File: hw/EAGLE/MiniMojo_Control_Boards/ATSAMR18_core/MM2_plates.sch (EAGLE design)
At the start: 54 parts, among them J1 CORTEX_DEBUGSMD, Q1 MOSFET-NCHANNEL2N7002PW, U1 3.3V, U2 EM406

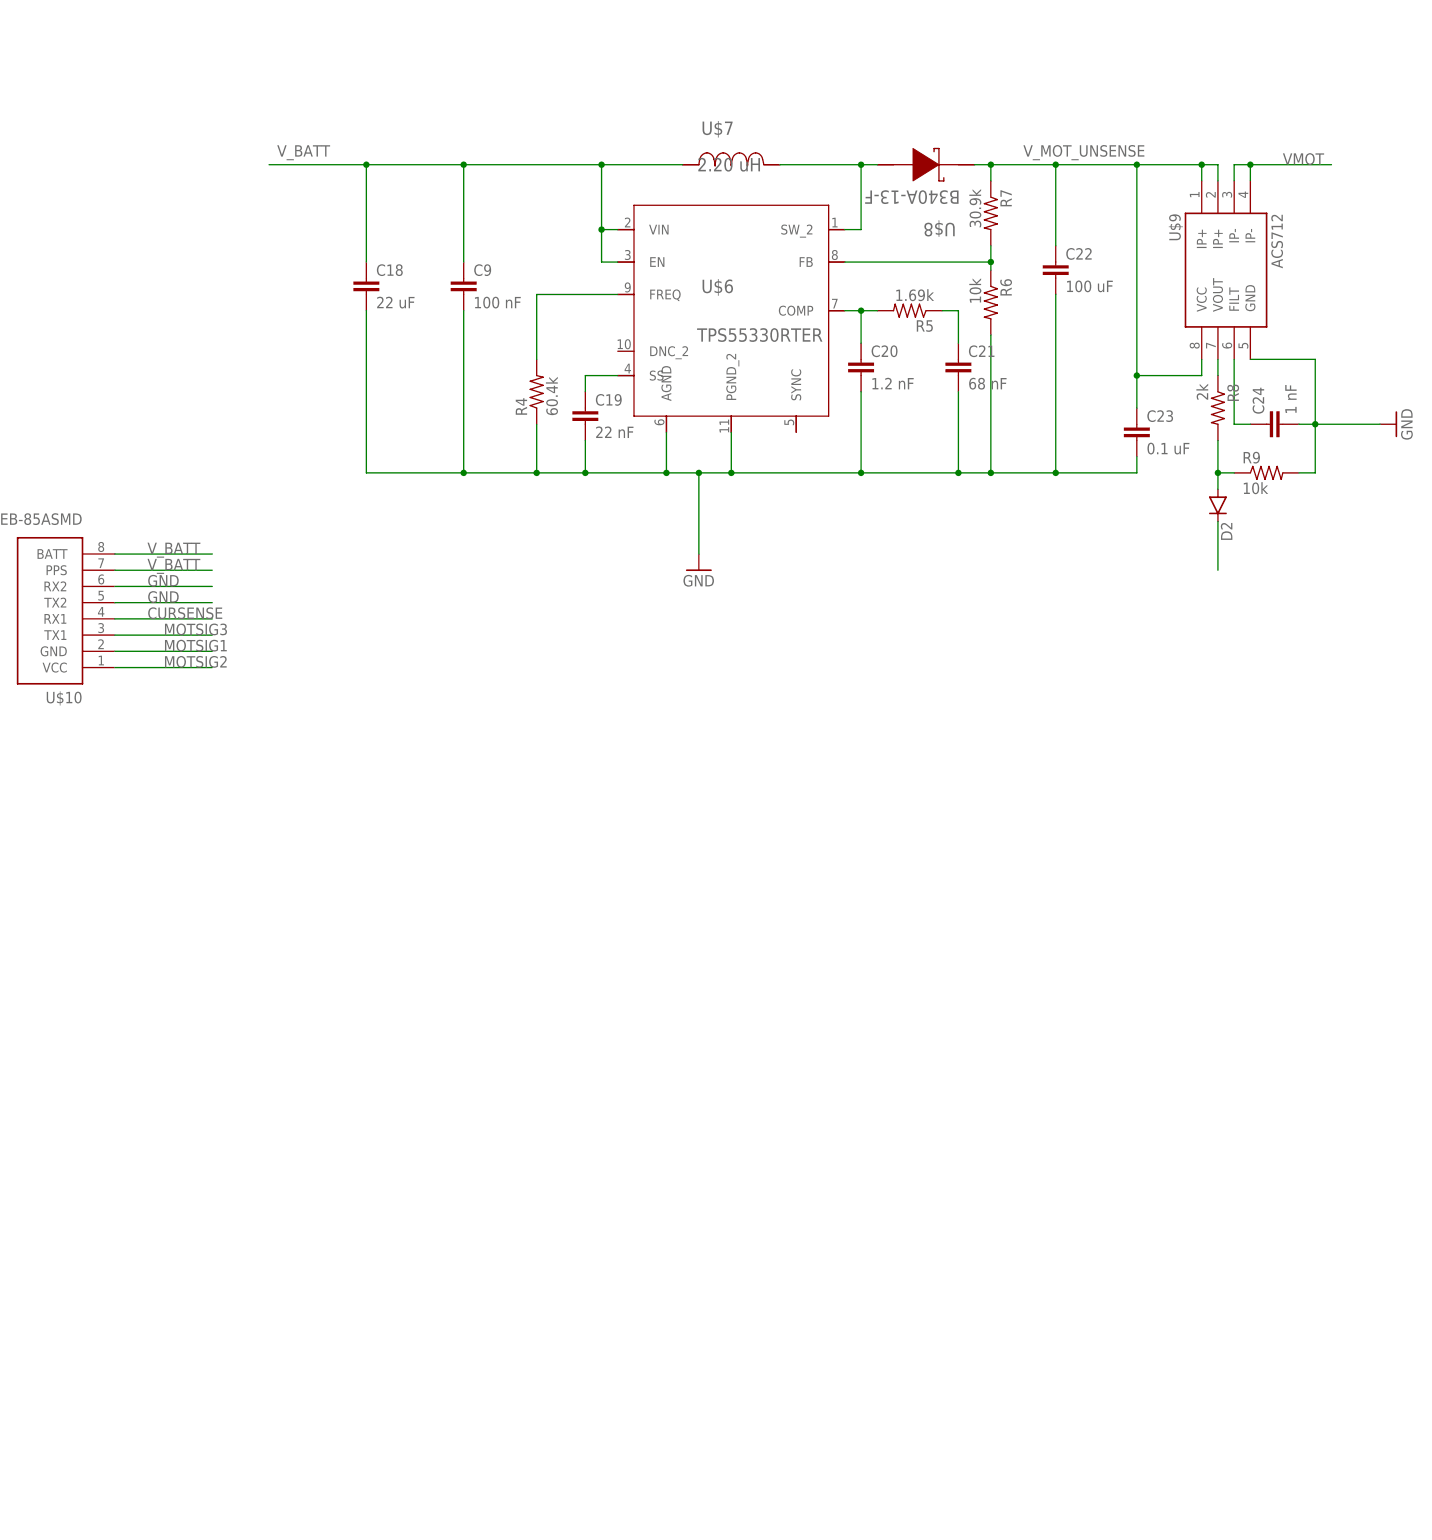
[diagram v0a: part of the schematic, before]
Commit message: Made TPS61089 mods
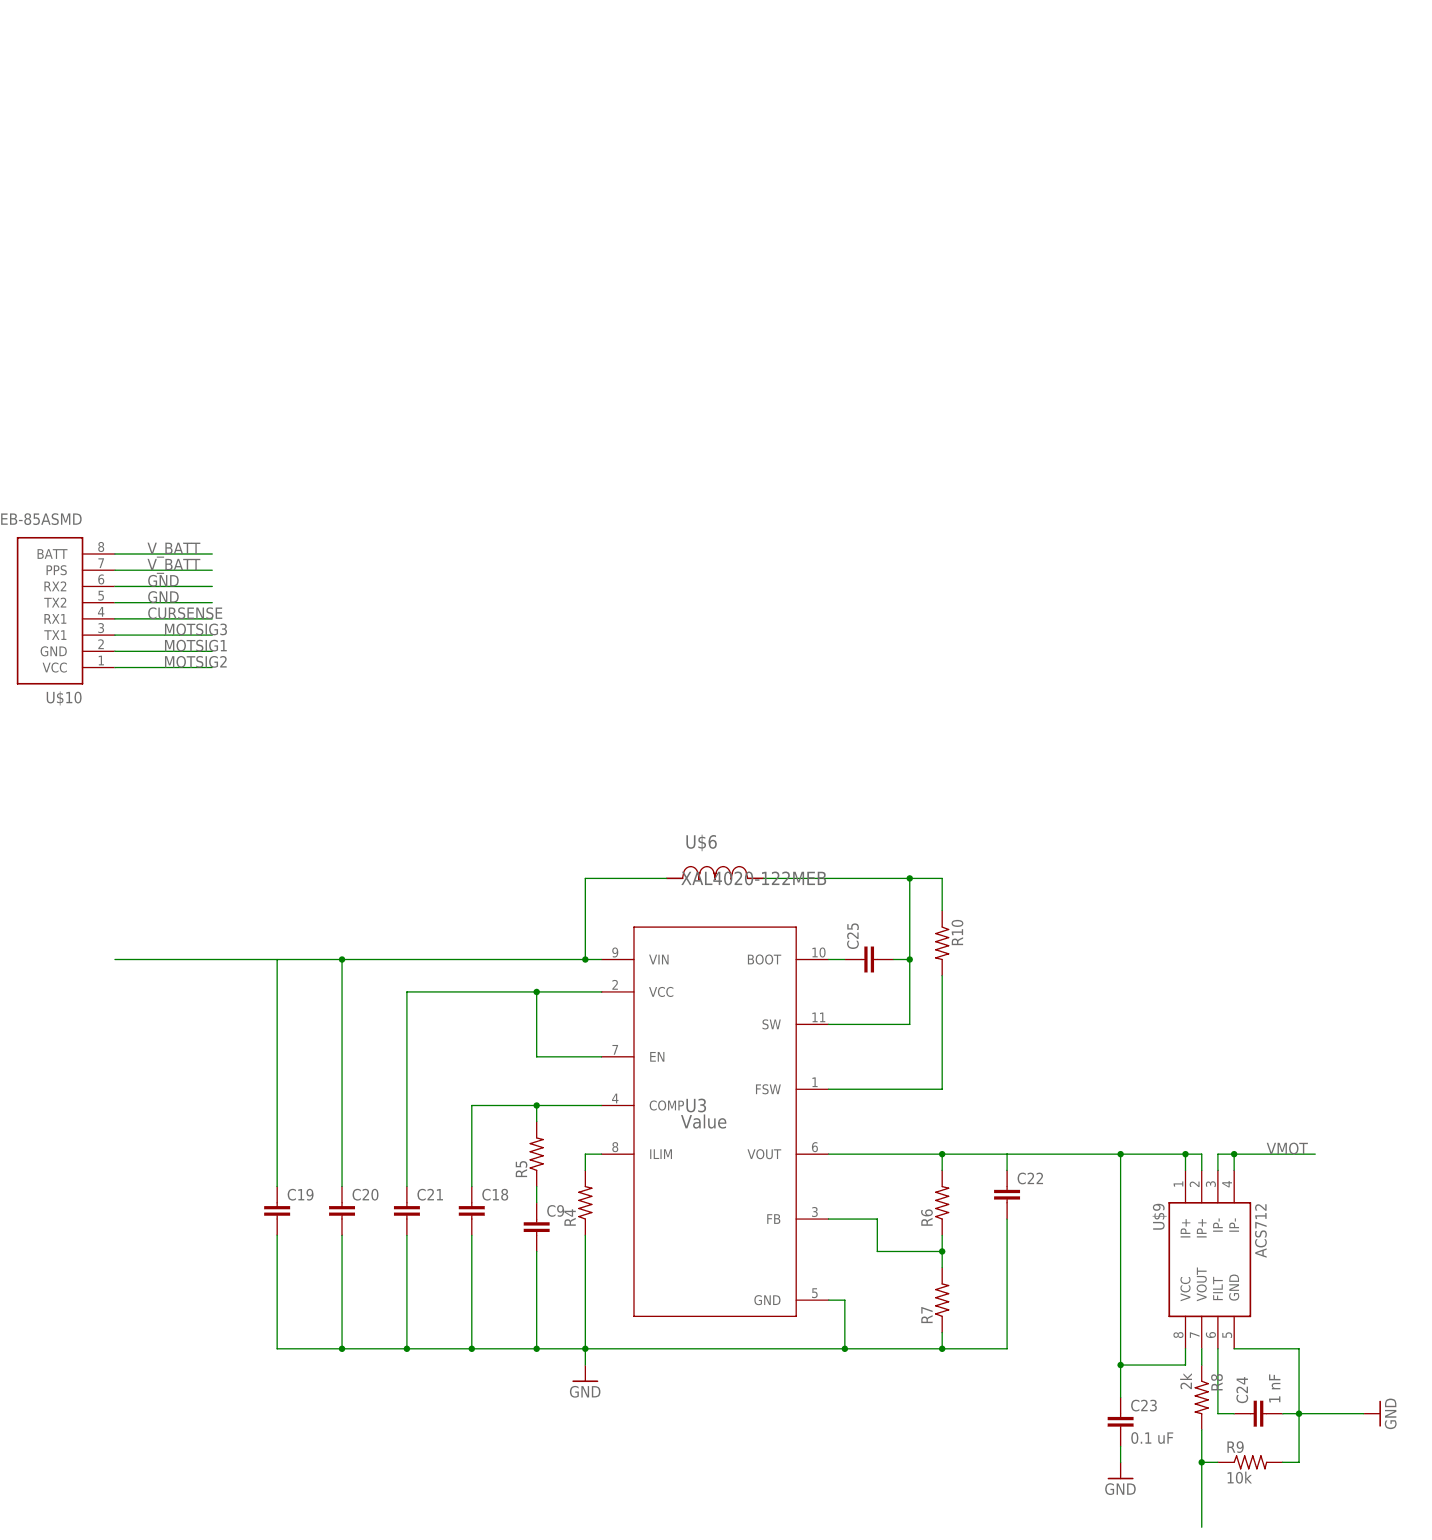
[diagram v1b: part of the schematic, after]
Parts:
- removed D2: (no value), SparkFun-DiscreteSemi:DIODESOD123
- removed U$7: 2.20 uH, TPS55330_libref:SRP4020-2R2M
- removed U$8: B340A-13-F, TPS55330_libref:B340A-13-F
- added C25: (no value), SparkFun-Passives:CAP0402-CAP
- added R10: (no value), SparkFun-Resistors:RESISTOR1206
- added U3: Value, TPS61089RNRR_4.8V:TPS61089RNRR
- C18: value 22 uF -> (none); device SparkFun-Passives:CAP1206 -> SparkFun-Passives:CAP0805
- C19: value 22 nF -> (none); device SparkFun-Passives:CAP0402-CAP -> SparkFun-Passives:CAP1206
- C20: value 1.2 nF -> (none)
- C21: value 68 nF -> (none); device SparkFun-Passives:CAP0402-CAP -> SparkFun-Passives:CAP0603-CAP
- C22: value 100 uF -> (none)
- C9: value 100 nF -> (none); device SparkFun-Passives:CAP0402-CAP -> SparkFun-Passives:CAP0805
- R4: value 60.4k -> (none); device SparkFun-Passives:RESISTOR0402-RES -> SparkFun-Resistors:RESISTOR1206
- R5: value 1.69k -> (none); device SparkFun-Passives:RESISTOR0402-RES -> SparkFun-Resistors:RESISTOR0402
- R6: value 10k -> (none); device SparkFun-Passives:RESISTOR0402-RES -> SparkFun-Resistors:RESISTOR0402
- R7: value 30.9k -> (none); device SparkFun-Passives:RESISTOR0402-RES -> SparkFun-Passives:RESISTOR0603-RES
- U$6: value TPS55330RTER -> XAL4020-122MEB; device TPS55330_libref:TPS55330RTER -> TPS61089RNRR_4.8V:XAL4020-122MEB
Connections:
- removed net N$13: C19.1, U$6.SS
- removed net N$18: R4.2, U$6.FREQ
- removed net N$4: U$6.SW_2, U$7.2, U$8.A
- removed net N$5: D2.A, R8.2, R9.1
- removed net N$9: C20.1, R5.2, U$6.COMP
- new net N$19: C21.1, U3.EN, U3.VCC
- new net N$27: C25.1, U3.BOOT
- new net N$28: C25.2, R10.1, U$6.2, U3.SW
- new net N$29: R10.2, U3.FSW
- new net N$3: R4.2, U3.ILIM
- new net N$31: R6.1, R7.2, U3.FB
- net CURSENSE: now also R8.2, R9.1; no longer D2.C
- net GND: now also R7.1, U3.GND; no longer R6.2, U$6.AGND, U$6.PGND_2
- net N$14: now also C9.1; no longer C21.1
- net N$15: now also C18.1, R5.2, U3.COMP; no longer R6.1, R7.2, U$6.FB
- net V_BATT: now also C19.1, C20.1, U$6.1, U3.VIN; no longer C18.1, C9.1, U$6.EN, U$6.VIN, U$7.1
- net V_MOT_UNSENSE: now also R6.2, U3.VOUT; no longer R7.1, U$8.K
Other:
- moved on the sheet: C18, C19, C20, C21, C22, C23, C24, C9, R4, R5, R6, R7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

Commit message: added TPS61089 w/ Tiny841
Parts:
- removed U$6: XAL4020-122MEB, TPS61089RNRR_4.8V:XAL4020-122MEB
- added J3: (no value), CSL_Components:M06SMD-1MM
- added Q2, Q3: MOSFET-NCHANNELAO3404A, SparkFun-DiscreteSemi:MOSFET-NCHANNELAO3404A
- added R11, R13, R14: 10k, SparkFun-Passives:RESISTOR0402-RES
- added U10: ATTINY84ATTINY84-20MU, SparkFun-DigitalIC:ATTINY84ATTINY84-20MU
- added U4: EM406, SparkFun-Connectors:EM406
- added Y1: 16MHZ, SparkFun-FreqCtrl:RESONATOR16MHZ
- C18: value (none) -> 62 pF
- C19, C22: value (none) -> 47 uF
- C20, C25: value (none) -> 100 nF
- C21: value (none) -> 2.2 uF
- C9: value (none) -> 1.2 nF
- R10: value (none) -> 523k
- R4: value (none) -> 143k
- R5: value (none) -> 22.6k; device SparkFun-Resistors:RESISTOR0402 -> SparkFun-Passives:RESISTOR0402-RES
- R6: value (none) -> 243k; device SparkFun-Resistors:RESISTOR0402 -> SparkFun-Passives:RESISTOR0402-RES
- R7: value (none) -> 82k
- R8: value 2k -> 10k
- U$1: value ATSAMR21E18A-MUT -> XAL4020-122MEB; device atmel-samr21:ATSAMR21E18A-MUT -> TPS61089RNRR_4.8V:XAL4020-122MEB
- U2: value EM406 -> ATSAMR21E18A-MUT; device SparkFun-Connectors:EM406 -> atmel-samr21:ATSAMR21E18A-MUT
- renumbered U$10 to U11, U$2 to U6, U$3 to U5, U$4 to U7, U$5 to U12, U$9 to U9, U3 to U8
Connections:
- removed net CURRENT_SIG1: U$1.PA06, U12.TX1
- removed net CURRENT_SIG2: U$1.PA07, U2.VCC
- removed net MOTSIG3: U11.TX1
- removed net N$12: U6.2
- removed net N$17: R8.1, U9.VOUT
- removed net SERVOB1: U$1.PA19, U2.GND2
- removed net SERVOB2: U$1.PA18, U2.TX
- removed net SERVOHIP: U$1.PA16, U2.RX
- removed net SERVOT1: U$1.PA08, U12.RX1
- removed net SERVOT2: U$1.PA09, U12.TX2
- new net MOTSIG0: U10.(PCINT10/INT0/OC0A/CKOUT)PB2, U11.BATT
- new net N$4: U10.(PCINT9/XTAL2)PB1, Y1.3
- new net N$5: U10.(PCINT8/XTAL1/CLKI)PB0, Y1.1
- new net SCL: J3.2, R9.1, U10.(PCINT4/T1/SCL/USCK/ADC4)PA4, U4.1PPS
- new net SCL_HV: Q2.D, U12.RX1, U12.TX1
- new net SCL_LV: Q2.S, R13.1, U2.PA09
- new net SDA: J3.4, R8.1, U10.(PCINT6/OC1A/SDA/MOSI/ADC6)PA6, U4.GND2
- new net SDA_HV: Q3.D, U12.GND, U12.VCC
- new net SDA_LV: Q3.S, R14.1, U2.PA08
- net 3.3V: now also Q2.G, Q3.G, R13.2, R14.2, U2.VDDIN, U2.VDDIO; no longer U$1.VDDIN, U$1.VDDIO
- net AVDD: now also U2.AVDD; no longer U$1.AVDD
- net BLINK: now also U2.PA17; no longer U$1.PA17
- net CURSENSE: now also U10.(PCINT1/AIN0/ADC1)PA1, U9.VOUT; no longer R8.2, R9.1, U11.RX1
- net DVDD: now also U2.DVDD; no longer U$1.DVDD
- net GND: now also J3.6, U10.GND, U11.RX1, U12.PPS, U2.GNDANA@1, U2.GNDANA@2, U2.GNDANA@3, U2.GNDANA@4, U2.GND_PAD, U4.RX, U4.TX, U6.2, Y1.2; no longer R9.2, U$1.GNDANA@1, U$1.GNDANA@2, U$1.GNDANA@3, U$1.GNDANA@4, U$1.GND_PAD, U11.RX2, U12.GND, U12.VCC, U2.1PPS, U2.GND1
- net MOTSIG1: now also U10.(PCINT7/ICP/OC0B/ADC7)PA7, U11.PPS; no longer U11.GND
- net MOTSIG2: now also J3.3, U10.(PCINT5/OC1B/MISO/DO/ADC5)PA5, U11.RX2; no longer U11.VCC
- net N$28: now also U$1.2; no longer U$6.2
- net PA24/USBDM: now also U12.RX2, U2.PA24; no longer U$1.PA24, U12.PPS
- net PA25/USBDP: now also U12.TX2, U2.PA25; no longer U$1.PA25, U12.RX2
- net RESET: now also J3.5, R11.1, U10.(PCINT11/~RESET/DW)PB3, U2.RESETN; no longer U$1.RESETN
- net RFN: now also U2.RFN; no longer U$1.RFN
- net RFP: now also U2.RFP; no longer U$1.RFP
- net SWCLK: now also U2.PA30; no longer U$1.PA30
- net SWDIO: now also U2.PA31; no longer U$1.PA31
- net VDDANA: now also U2.VDDANA@1; no longer U$1.VDDANA@1
- net VDDCORE: now also U2.VDDCORE; no longer U$1.VDDCORE
- net VMOT: now also J3.1, R11.2, R8.2, R9.2, U10.VCC, U11.GND, U11.TX1, U11.VCC
- net V_BATT: now also U$1.1, U4.GND1, U4.VCC; no longer U$6.1, U11.BATT, U11.PPS
- net XIN: now also U2.XTAL2; no longer U$1.XTAL2
- net XOUT: now also U2.XTAL1; no longer U$1.XTAL1
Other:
- moved on the sheet: R8, R9
